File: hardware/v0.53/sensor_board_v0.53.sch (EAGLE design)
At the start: 58 parts, among them J3 USB-MICROB, J6 AVR_SPI_PRG_6PTH, U1 ATMEGA328P, U10 TSL2591, U3 OPA344, U4 RFM69HW, U5 FT231XS, U6 ADMP401, U8 MCP1703CB, U9 BMP280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

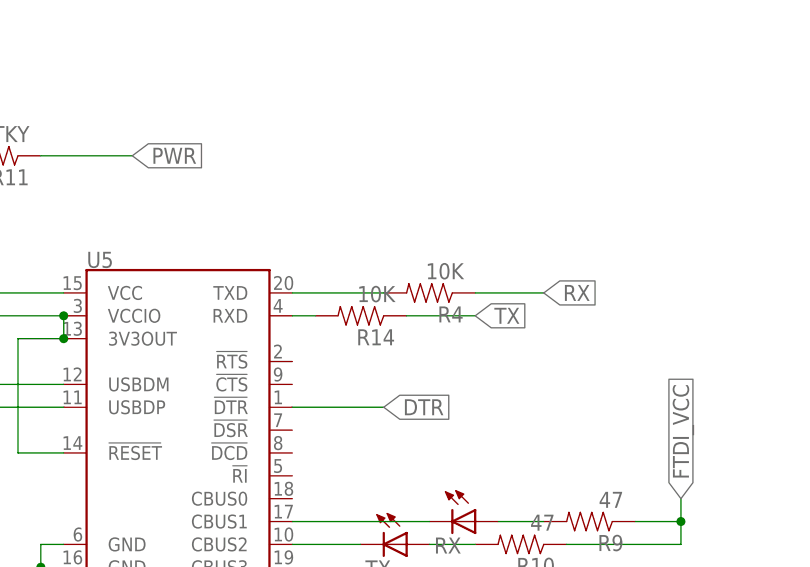
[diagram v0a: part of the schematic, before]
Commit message: Fixed attributes
Updated MPN for 1K ohm resistor
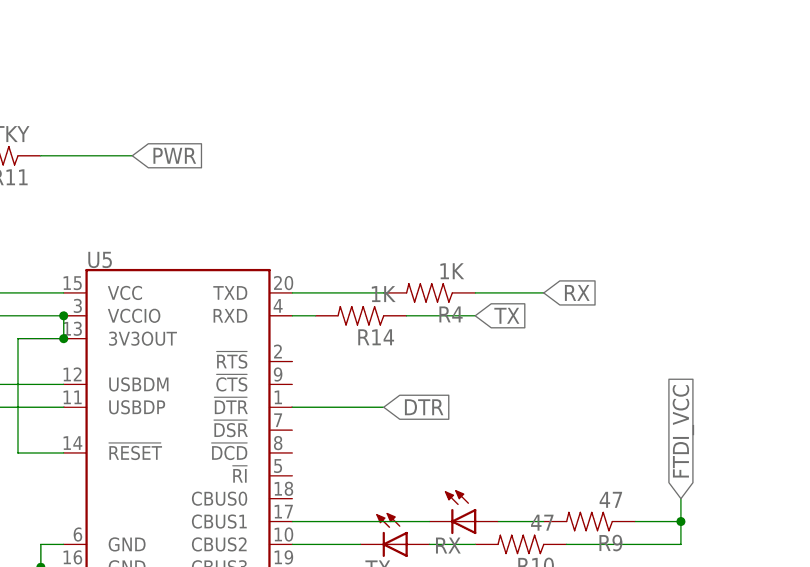
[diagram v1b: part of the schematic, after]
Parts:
- R14, R4: value 10K -> 1K; MPN RC0805FR-0710KL -> RC0805FR-071KL
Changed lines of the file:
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@@
 <part name="J6" library="SparkFun-Connectors" deviceset="AVR_SPI_PRG_6" device="PTH"/>
 <part name="J2" library="SparkFun-Connectors" deviceset="M04" device="PTH"/>
-<part name="R4" library="SparkFun-Passives" deviceset="RESISTOR" device="0805-RES" value="10K">
-<attribute name="MPN" value="RC0805FR-0710KL"/>
+<part name="R4" library="SparkFun-Passives" deviceset="RESISTOR" device="0805-RES" value="1K">
+<attribute name="MPN" value="RC0805FR-071KL"/>
 </part>
-<part name="R14" library="SparkFun-Passives" deviceset="RESISTOR" device="0805-RES" value="10K">
-<attribute name="MPN" value="RC0805FR-0710KL"/>
+<part name="R14" library="SparkFun-Passives" deviceset="RESISTOR" device="0805-RES" value="1K">
+<attribute name="MPN" value="RC0805FR-071KL"/>
 </part>
 </parts>
